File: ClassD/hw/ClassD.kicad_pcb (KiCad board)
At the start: 2 copper layers, 63 parts, among them P1 RedRCA, P2 WhiteRCA, P3 CONN_01X02, P4 CONN_01X02, P5 CONN_01X02, SW1 SW_PUSH, SW2 SW_PUSH, U1 TDA7491LP, U2 MCP1700T

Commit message: Initial Layout Setup
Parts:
- moved FB5 46.6 mm to (227.4, 155.9)
- moved FB1 46.6 mm to (235.5, 160.6)
- moved FB2 46.6 mm to (238.3, 156.3)
- moved FB3 46.6 mm to (230.1, 162.2)
- moved FB4 46.6 mm to (231.2, 156.8)
- moved FB6 46.6 mm to (236.2, 151.3)
- moved FB7 46.6 mm to (230.2, 151.8)
- moved FB8 46.6 mm to (232.9, 155.6)
- moved C3 27.8 mm to (149.9, 105.4), turned to 270 degrees
- moved C4 26.8 mm to (148.6, 110.5)
- moved C14 25.4 mm to (180.3, 130.9)
- moved R5 25.4 mm to (178.1, 126.9)
- moved C12 25.4 mm to (176.6, 131.5)
- moved R6 25.4 mm to (173.0, 128.0)
- moved P1 24.8 mm to (137.2, 104.1), turned to 90 degrees
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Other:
- net class Default: clearance 0.2 -> 0.3048; trace_width 0.25 -> 0.3048; via_dia 0.6 -> 0.6858; via_drill 0.4 -> 0.3302
- rule trace_clearance: 0.2 -> 0.3048
- rule trace_min: 0.2 -> 0.1524
- rule via_min_drill: 0.3 -> 0.3302
- rule via_min_size: 0.4 -> 0.6858
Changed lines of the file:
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@@
-(kicad_pcb (version 4) (host pcbnew 4.0.1-3.201512221402+6198~38~ubuntu14.04.1-stable)
+(kicad_pcb (version 4) (host pcbnew 0.201508060901+6055~28~ubuntu14.04.1-product)
   (general
     (links 129)
     (no_connects 129)
-    (area 0 0 0 0)
+    (area 72.302 69.551 273.562881 166.4065)
     (thickness 1.6)
     (drawings 0)
@@
   )
   (setup
-    (last_trace_width 0.25)
-    (trace_clearance 0.2)
+    (last_trace_width 0.3048)
+    (user_trace_width 0.1524)
+    (user_trace_width 0.3048)
+    (user_trace_width 0.6096)
+    (trace_clearance 0.3048)
     (zone_clearance 0.508)
     (zone_45_only no)
-    (trace_min 0.2)
+    (trace_min 0.1524)
     (segment_width 0.2)
     (edge_width 0.15)
-    (via_size 0.6)
-    (via_drill 0.4)
-    (via_min_size 0.4)
-    (via_min_drill 0.3)
-    (uvia_size 0.3)
-    (uvia_drill 0.1)
+    (via_size 0.6858)
+    (via_drill 0.3302)
+    (via_min_size 0.6858)
+    (via_min_drill 0.3302)
+    (user_via 1.27 0.6096)
+    (uvia_size 0.254)
+    (uvia_drill 0.127)
     (uvias_allowed no)
-    (uvia_min_size 0.2)
-    (uvia_min_drill 0.1)
+    (uvia_min_size 0.254)
+    (uvia_min_drill 0.127)
     (pcb_text_width 0.3)
     (pcb_text_size 1.5 1.5)
@@
   (net 39 "Net-(D1-Pad1)")
   (net_class Default "This is the default net class."
-    (clearance 0.2)
-    (trace_width 0.25)
-    (via_dia 0.6)
-    (via_drill 0.4)
-    (uvia_dia 0.3)
-    (uvia_drill 0.1)
+    (clearance 0.3048)
+    (trace_width 0.3048)
+    (via_dia 0.6858)
+    (via_drill 0.3302)
+    (uvia_dia 0.254)
+    (uvia_drill 0.127)
     (add_net /3V3)
     (add_net /DIAG)
@@
   )
   (module Capacitors_SMD:C_1206_HandSoldering (layer F.Cu)
-    (at 122.8725 90.6145)
+    (at 143.51 104.14)
     (descr "Capacitor SMD 1206, hand soldering")
     (tags "capacitor 1206")
@@
   )
   (module Capacitors_SMD:C_1206 (layer F.Cu)
-    (at 122.8725 96.0755)
+    (at 142.24 110.49)
     (descr "Capacitor SMD 1206, reflow soldering, AVX (see smccp.pdf)")
     (tags "capacitor 1206")
@@
   )
   (module Capacitors_SMD:C_0805 (layer F.Cu)
-    (at 122.555 100.1395)
+    (at 149.86 105.41 270)
     (descr "Capacitor SMD 0805, reflow soldering, AVX (see smccp.pdf)")
     (tags "capacitor 0805")
     (attr smd)
-    (fp_text reference C3 (at 0 -2.1) (layer F.SilkS)
-      (effects (font (size 1 1) (thickness 0.15)))
-    )
-    (fp_text value 1N (at 0 2.1) (layer F.Fab)
+    (fp_text reference C3 (at 0 -2.1 270) (layer F.SilkS)
+      (effects (font (size 1 1) (thickness 0.15)))
+    )
+    (fp_text value 1N (at 0 2.1 270) (layer F.Fab)
       (effects (font (size 1 1) (thickness 0.15)))
     )
@@
     (fp_line (start 0.5 -0.85) (end -0.5 -0.85) (layer F.SilkS) (width 0.15))
     (fp_line (start -0.5 0.85) (end 0.5 0.85) (layer F.SilkS) (width 0.15))
-    (pad 1 smd rect (at -1 0) (size 1 1.25) (layers F.Cu F.Paste F.Mask)
+    (pad 1 smd rect (at -1 0 270) (size 1 1.25) (layers F.Cu F.Paste F.Mask)
       (net 2 "Net-(C1-Pad2)"))
-    (pad 2 smd rect (at 1 0) (size 1 1.25) (layers F.Cu F.Paste F.Mask)
+    (pad 2 smd rect (at 1 0 270) (size 1 1.25) (layers F.Cu F.Paste F.Mask)
       (net 5 OGND))
     (model Capacitors_SMD.3dshapes/C_0805.wrl
@@
   )
   (module Capacitors_SMD:C_0805 (layer F.Cu)
-    (at 122.428 104.902)
+    (at 148.59 110.49)
     (descr "Capacitor SMD 0805, reflow soldering, AVX (see smccp.pdf)")
     (tags "capacitor 0805")
@@
   )
   (module Capacitors_SMD:C_0805 (layer F.Cu)
-    (at 156.2735 116.2685)
+    (at 176.5935 131.5085)
     (descr "Capacitor SMD 0805, reflow soldering, AVX (see smccp.pdf)")
     (tags "capacitor 0805")
@@
   )
   (module Capacitors_SMD:C_0805 (layer F.Cu)
-    (at 159.9565 115.6335)
+    (at 180.2765 130.8735)
     (descr "Capacitor SMD 0805, reflow soldering, AVX (see smccp.pdf)")
     (tags "capacitor 0805")
@@
   )
   (module ClassD:RCJ1x (layer F.Cu)
-    (at 112.395 103.124)
-    (fp_text reference P1 (at 0 6.35) (layer F.SilkS)
-      (effects (font (size 1 1) (thickness 0.15)))
-    )
-    (fp_text value RedRCA (at 0 -5.08) (layer F.Fab)
+    (at 137.16 104.14 90)
+    (fp_text reference P1 (at 0 6.35 90) (layer F.SilkS)
+      (effects (font (size 1 1) (thickness 0.15)))
+    )
+    (fp_text value RedRCA (at 0 -5.08 90) (layer F.Fab)
       (effects (font (size 1 1) (thickness 0.15)))
     )
@@
     (fp_line (start -3 -7) (end -5 -7) (layer Eco1.User) (width 0.15))
     (fp_line (start -5 -7) (end -5 -4) (layer Eco1.User) (width 0.15))
-    (pad 2 thru_hole circle (at 0 0) (size 2.7 2.7) (drill 1.7) (layers *.Cu *.Mask F.SilkS)
+    (pad 2 thru_hole circle (at 0 0 90) (size 2.7 2.7) (drill 1.7) (layers *.Cu *.Mask F.SilkS)
       (net 1 "Net-(C1-Pad1)"))
-    (pad 1 thru_hole circle (at 0 -4.5) (size 4 4) (drill 2.6) (layers *.Cu *.Mask F.SilkS)
+    (pad 1 thru_hole circle (at 0 -4.5 90) (size 4 4) (drill 2.6) (layers *.Cu *.Mask F.SilkS)
       (net 3 "Net-(C2-Pad1)"))
-    (pad 1 thru_hole circle (at 5 0) (size 4 4) (drill 2.6) (layers *.Cu *.Mask F.SilkS)
+    (pad 1 thru_hole circle (at 5 0 90) (size 4 4) (drill 2.6) (layers *.Cu *.Mask F.SilkS)
       (net 3 "Net-(C2-Pad1)"))
-    (pad 1 thru_hole circle (at -5 0) (size 4 4) (drill 2.6) (layers *.Cu *.Mask F.SilkS)
+    (pad 1 thru_hole circle (at -5 0 90) (size 4 4) (drill 2.6) (layers *.Cu *.Mask F.SilkS)
       (net 3 "Net-(C2-Pad1)"))
   )
@@
   )
   (module Resistors_SMD:R_0805 (layer F.Cu)
-    (at 157.7975 111.633)
+    (at 178.1175 126.873)
     (descr "Resistor SMD 0805, reflow soldering, Vishay (see dcrcw.pdf)")
     (tags "resistor 0805")
@@
   )
   (module Resistors_SMD:R_0805 (layer F.Cu)
-    (at 152.7175 112.7125)
+    (at 173.0375 127.9525)
     (descr "Resistor SMD 0805, reflow soldering, Vishay (see dcrcw.pdf)")
     (tags "resistor 0805")
@@
   )
   (module ClassD:PowerSSO36-EPD (layer F.Cu)
-    (at 175.26 111.5695)
+    (at 163.83 115.57)
     (fp_text reference U1 (at 6 12.2) (layer F.SilkS)
       (effects (font (size 1 1) (thickness 0.15)))
@@
   )
   (module Resistors_SMD:R_0805 (layer F.Cu)
-    (at 193.6115 140.2715)
+    (at 235.5215 160.5915)
     (descr "Resistor SMD 0805, reflow soldering, Vishay (see dcrcw.pdf)")
     (tags "resistor 0805")
@@
   )
   (module Resistors_SMD:R_0805 (layer F.Cu)
-    (at 196.4055 136.017)
+    (at 238.3155 156.337)
     (descr "Resistor SMD 0805, reflow soldering, Vishay (see dcrcw.pdf)")
     (tags "resistor 0805")
@@
   )
   (module Resistors_SMD:R_0805 (layer F.Cu)
-    (at 188.214 141.9225)
+    (at 230.124 162.2425)
     (descr "Resistor SMD 0805, reflow soldering, Vishay (see dcrcw.pdf)")
     (tags "resistor 0805")
@@
   )
   (module Resistors_SMD:R_0805 (layer F.Cu)
-    (at 189.2935 136.525)
+    (at 231.2035 156.845)
     (descr "Resistor SMD 0805, reflow soldering, Vishay (see dcrcw.pdf)")
     (tags "resistor 0805")
@@
   )
   (module Resistors_SMD:R_0805 (layer F.Cu)
-    (at 185.4835 135.5725)
+    (at 227.3935 155.8925)
     (descr "Resistor SMD 0805, reflow soldering, Vishay (see dcrcw.pdf)")
     (tags "resistor 0805")
@@
   )
   (module Resistors_SMD:R_0805 (layer F.Cu)
-    (at 194.31 130.937)
+    (at 236.22 151.257)
     (descr "Resistor SMD 0805, reflow soldering, Vishay (see dcrcw.pdf)")
     (tags "resistor 0805")
@@
   )
   (module Resistors_SMD:R_0805 (layer F.Cu)
-    (at 188.2775 131.445)
+    (at 230.1875 151.765)
     (descr "Resistor SMD 0805, reflow soldering, Vishay (see dcrcw.pdf)")
     (tags "resistor 0805")
@@
   )
   (module Resistors_SMD:R_0805 (layer F.Cu)
-    (at 191.008 135.3185)
+    (at 232.918 155.6385)
     (descr "Resistor SMD 0805, reflow soldering, Vishay (see dcrcw.pdf)")
     (tags "resistor 0805")

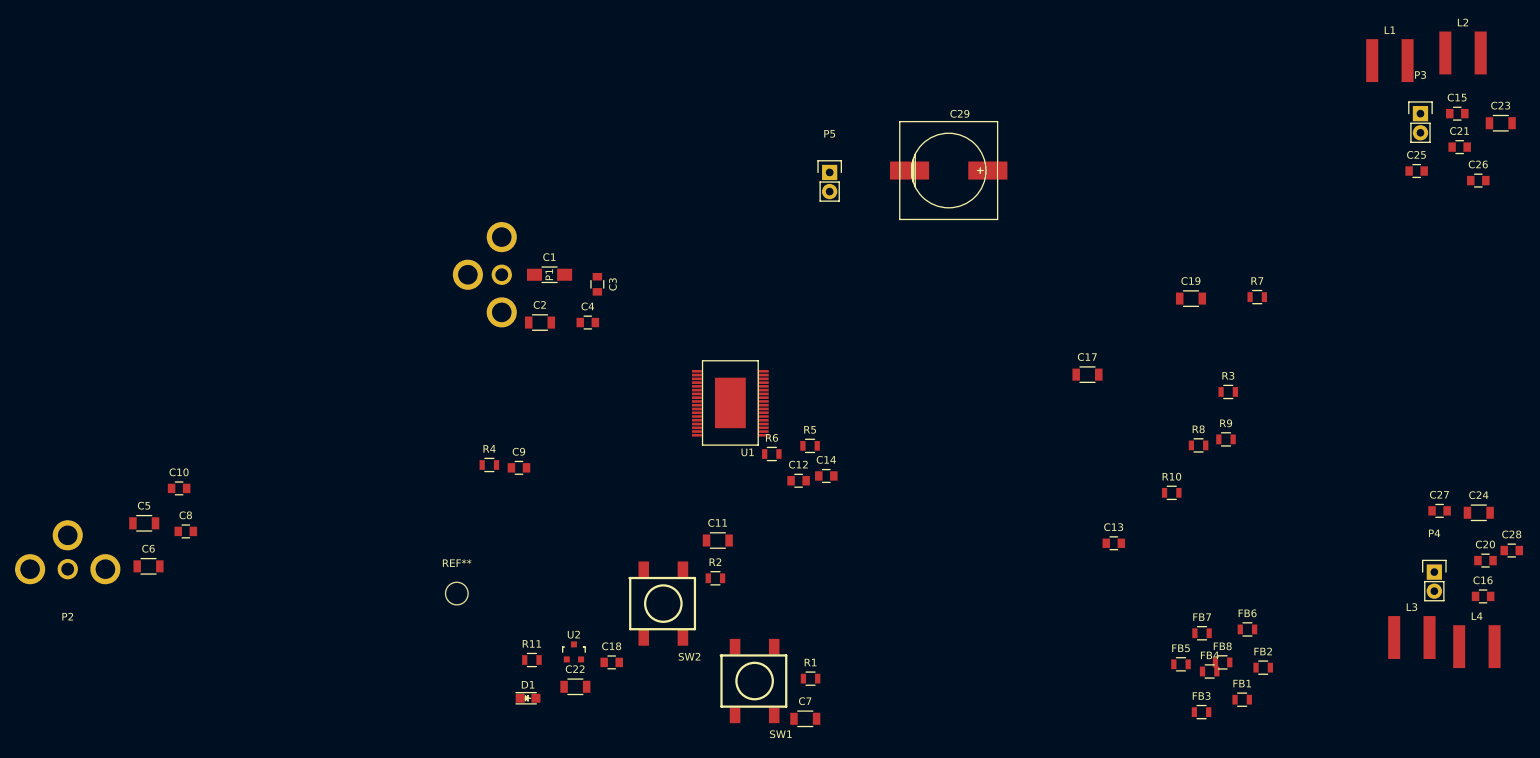
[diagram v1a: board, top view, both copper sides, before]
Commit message: Placed RCA jacks, buttons and left side components
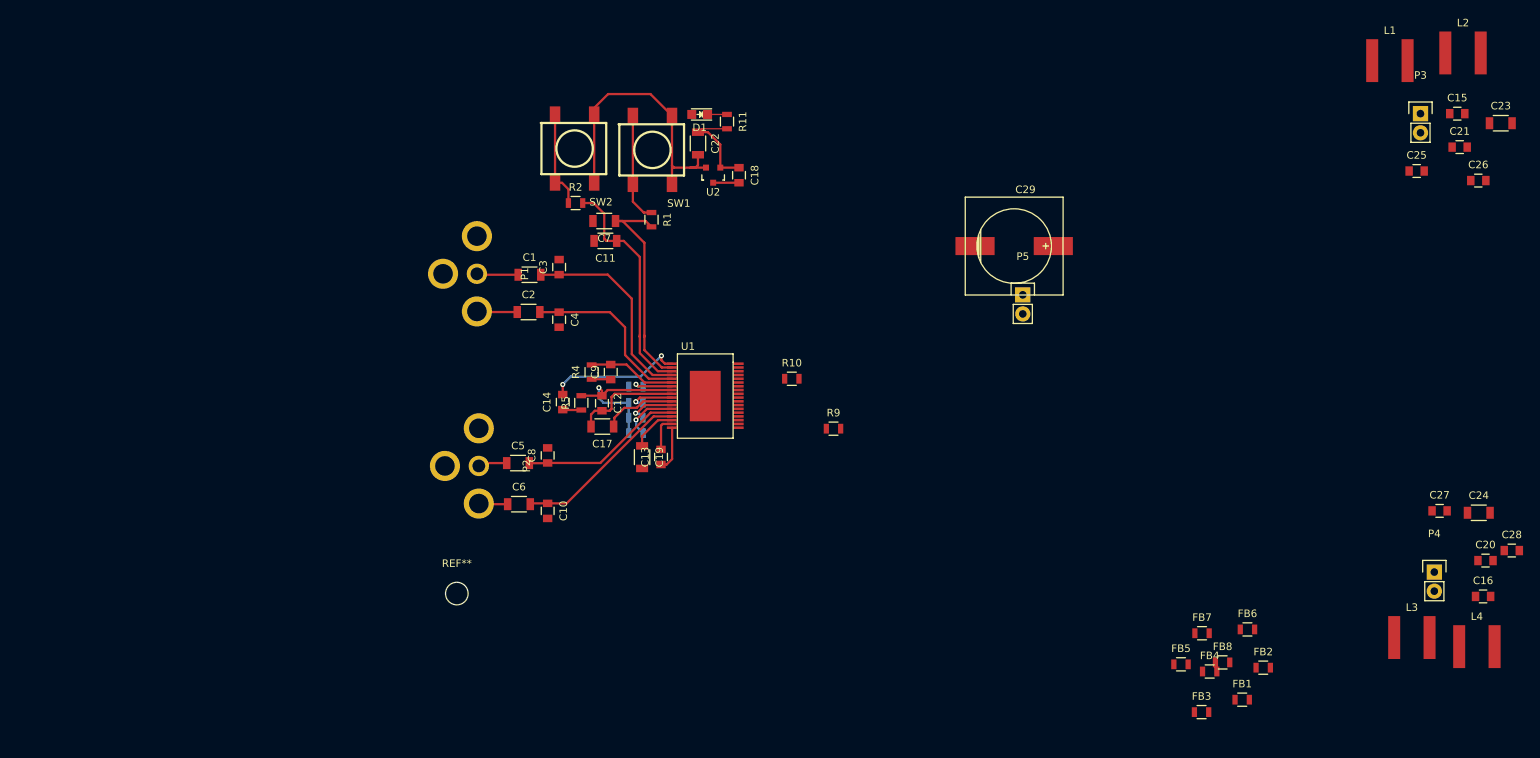
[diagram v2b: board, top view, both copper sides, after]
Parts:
- C1: footprint Capacitors_SMD:C_1206_HandSoldering -> Capacitors_SMD:C_1206
- R3, R6, R7, R8: moved to B.Cu
- moved R7 84.1 mm to (155.0, 123.1)
- moved D1 80.8 mm to (163.4, 82.8), turned to 180 degrees
- moved R3 78.7 mm to (155.0, 119.0)
- moved R11 76.1 mm to (167.1, 83.8), turned to 270 degrees
- moved C19 75.9 mm to (155.8, 128.4), turned to 270 degrees
- moved R8 74.7 mm to (155.0, 125.2)
- moved C22 74.0 mm to (163.2, 86.7), turned to 270 degrees
- moved SW1 71.9 mm to (157.2, 87.6)
- moved C7 71.3 mm to (150.8, 97.0), turned to 180 degrees
- moved C18 66.9 mm to (168.7, 90.9), turned to 270 degrees
- moved U2 66.0 mm to (165.2, 90.9), turned to 180 degrees
- moved C17 64.8 mm to (150.5, 124.3), turned to 180 degrees
- moved R1 64.5 mm to (157.0, 96.8), turned to 270 degrees
- moved SW2 61.6 mm to (146.8, 87.4)
- moved C13 61.2 mm to (158.3, 128.3), turned to 90 degrees
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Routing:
- net /3V3: track 0.00 -> 38.5 mm
- net /MUTE: track 0.00 -> 30.8 mm
- net /STBY: track 0.00 -> 29.1 mm
- net Net-(C1-Pad2): track 0.00 -> 27.3 mm
- net Net-(C10-Pad1): track 0.00 -> 23.7 mm
- net Net-(C2-Pad2): track 0.00 -> 23.4 mm
- net /VDDS: track 0.00 -> 23.2 mm, vias 0 -> 1
- net Net-(C5-Pad2): track 0.00 -> 21.8 mm
- net Net-(C14-Pad2): track 0.00 -> 18.2 mm, vias 0 -> 2
- net OGND: track 0.00 -> 15.8 mm
- net Net-(R1-Pad1): track 0.00 -> 14.5 mm
- net SGND: track 0.00 -> 14.4 mm
- net Net-(R2-Pad1): track 0.00 -> 13.1 mm
- net Net-(C9-Pad2): track 0.00 -> 11.7 mm
- net Net-(C17-Pad1): track 0.00 -> 9.79 mm
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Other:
- net class Default: clearance 0.3048 -> 0.1524
- rule trace_clearance: 0.3048 -> 0.1524

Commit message: Finished output filters (right side)
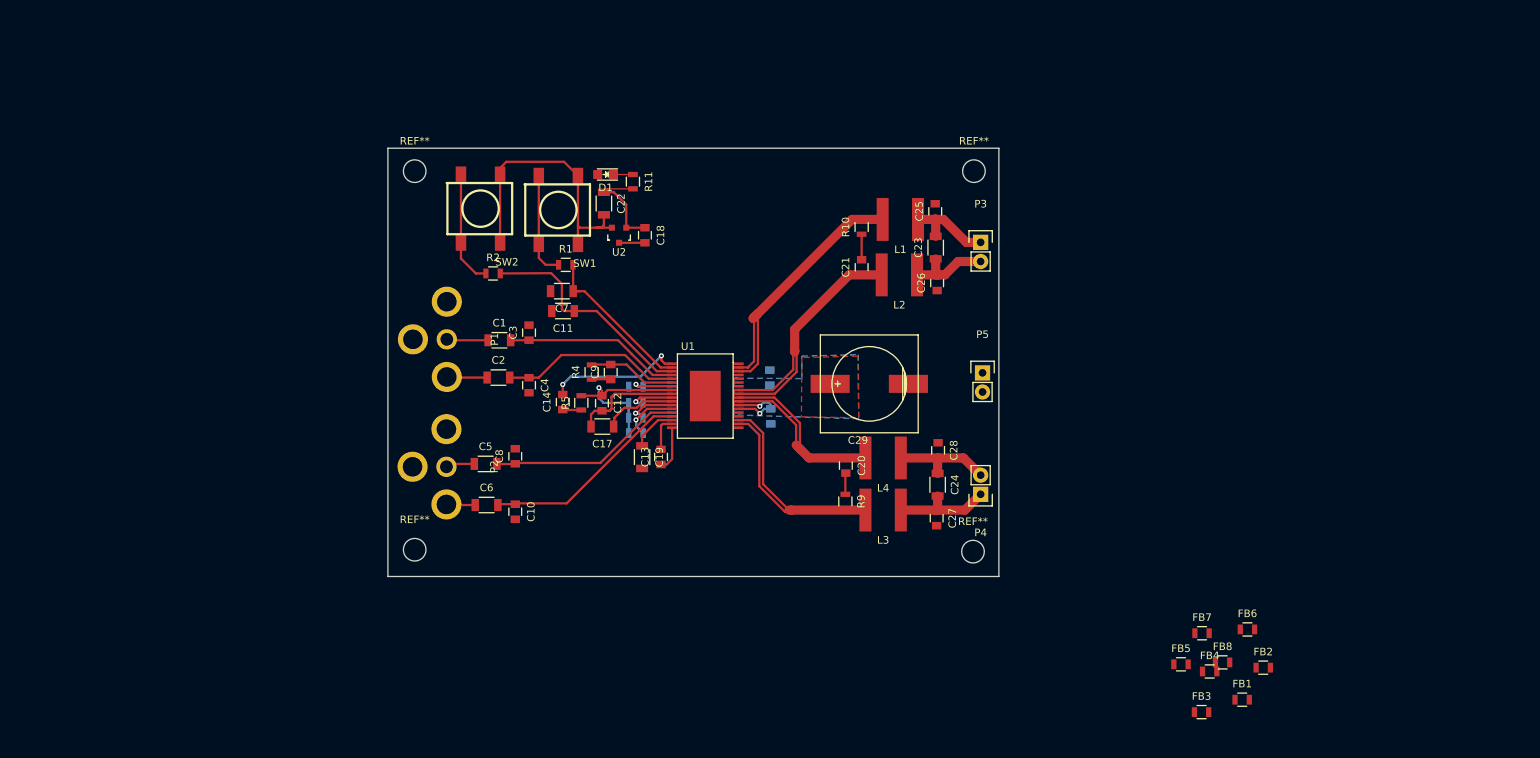
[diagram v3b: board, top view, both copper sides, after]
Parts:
- added REF**: MountingHole_3mm, Mounting_Holes:MountingHole_3mm, F.Cu at (199.9, 90.4)
- added REF**: MountingHole_3mm, Mounting_Holes:MountingHole_3mm, F.Cu at (199.8, 140.9)
- added REF**: MountingHole_3mm, Mounting_Holes:MountingHole_3mm, F.Cu at (125.6, 90.4)
- C15, C16: moved to B.Cu
- moved C15 97.8 mm to (172.8, 117.8), turned to 270 degrees
- moved C16 97.6 mm to (172.9, 123.0), turned to 270 degrees
- moved C20 85.9 mm to (182.9, 129.5), turned to 270 degrees
- moved L4 82.8 mm to (187.8, 128.5), turned to 180 degrees
- moved C21 81.0 mm to (185.0, 103.1), turned to 90 degrees
- moved L2 80.5 mm to (190.0, 104.2), turned to 180 degrees
- moved C28 77.4 mm to (195.1, 127.5), turned to 270 degrees
- moved C23 76.9 mm to (194.8, 100.5), turned to 90 degrees
- moved C26 73.2 mm to (195.0, 105.2), turned to 90 degrees
- moved L3 72.3 mm to (187.8, 135.4), turned to 180 degrees
- moved C24 72.0 mm to (195.1, 132.0), turned to 270 degrees
- moved L1 68.4 mm to (190.1, 96.8), turned to 180 degrees
- moved C27 66.8 mm to (194.9, 136.5), turned to 270 degrees
- moved C25 64.2 mm to (194.7, 95.7), turned to 90 degrees
- moved P4 61.2 mm to (200.8, 133.3), turned to 180 degrees
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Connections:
- C10 pad 2: OGND -> GND
- C11 pad 2: OGND -> GND
- C18 pad 1: OGND -> GND
- C19 pad 2: OGND -> GND
- C22 pad 1: OGND -> GND
- C3 pad 2: OGND -> GND
- C4 pad 2: OGND -> GND
- C7 pad 2: OGND -> GND
- C8 pad 2: OGND -> GND
- C9 pad 1: OGND -> GND
- FB1 pad 1: OGND -> GND
- FB2 pad 1: OGND -> GND
- FB3 pad 1: OGND -> GND
- FB4 pad 1: OGND -> GND
- FB5 pad 1: OGND -> GND
- FB6 pad 1: OGND -> GND
- FB7 pad 1: OGND -> GND
- FB8 pad 1: OGND -> GND
- R11 pad 2: OGND -> GND
- R3 pad 1: OGND -> GND
- R4 pad 1: OGND -> GND
- U1 pad 1: OGND -> GND
- U2 pad 1: OGND -> GND
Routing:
- net Net-(L1-Pad2): track 0.00 -> 42.8 mm
- net Net-(L3-Pad2): track 0.00 -> 41.8 mm
- net Net-(C20-Pad1): track 0.00 -> 34.6 mm
- net Net-(C21-Pad1): track 0.00 -> 28.1 mm
- net /VCC: track 3.44 -> 26.1 mm, vias 0 -> 2
- net GND: track 0.00 -> 15.8 mm
- net OGND: track 15.8 -> 0.00 mm
- net /OUTR-: track 0.00 -> 13.6 mm
- net /OUTR+: track 0.00 -> 13.5 mm
- net /OUTL+: track 0.00 -> 11.9 mm
- net /OUTL-: track 0.00 -> 11.5 mm
- net /STBY: track 29.1 -> 21.8 mm
- net Net-(C5-Pad2): track 21.8 -> 26.3 mm
- net Net-(C10-Pad1): track 23.7 -> 28.0 mm
- net Net-(C1-Pad2): track 27.3 -> 23.4 mm
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- added copper zone on B.Cu, net /VCC
- added copper zone on F.Cu, net /VCC
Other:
- board outline added: 81.2 x 56.9 mm
